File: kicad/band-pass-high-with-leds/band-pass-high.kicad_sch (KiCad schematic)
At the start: 66 parts, among them J1 Conn_01x06

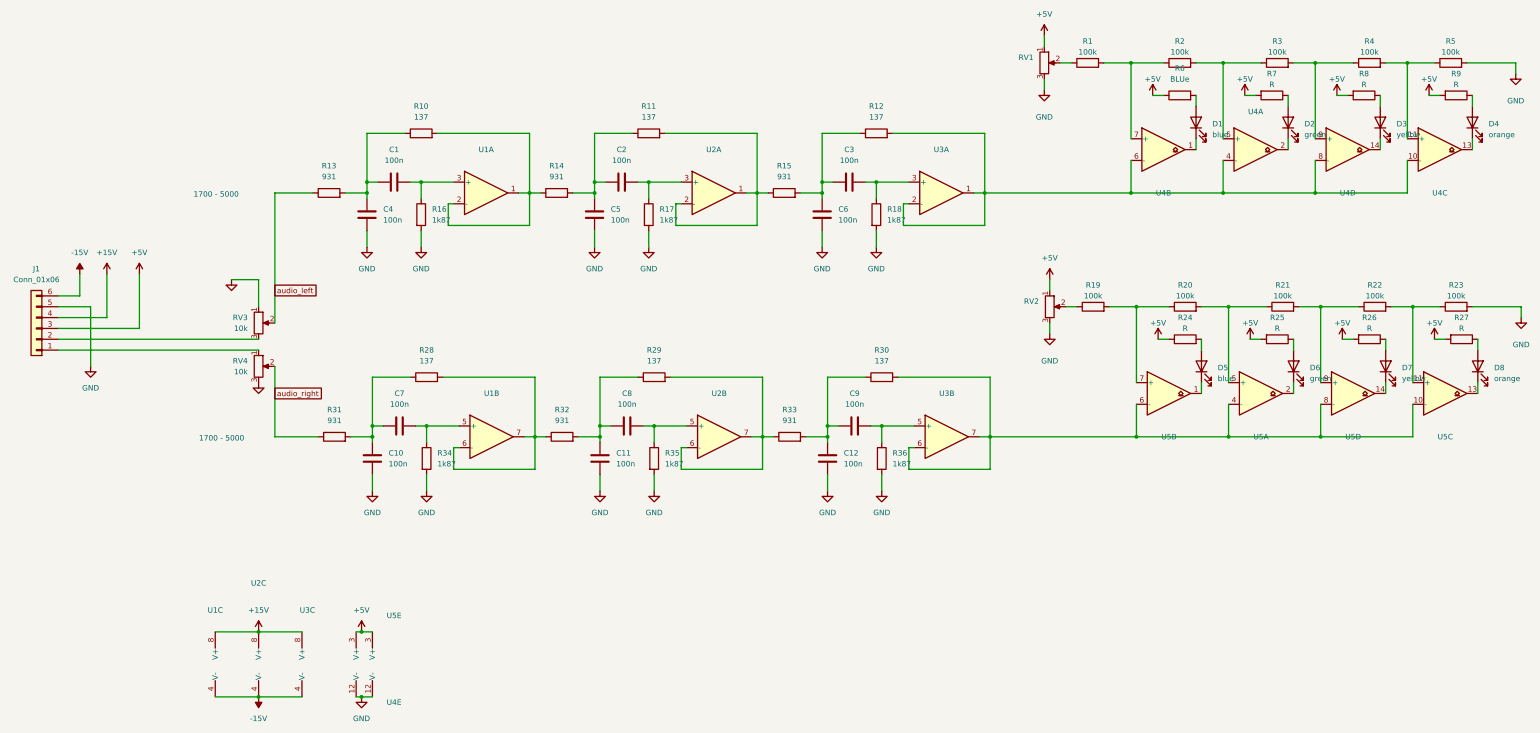
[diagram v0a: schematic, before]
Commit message: Made a filter PCB design
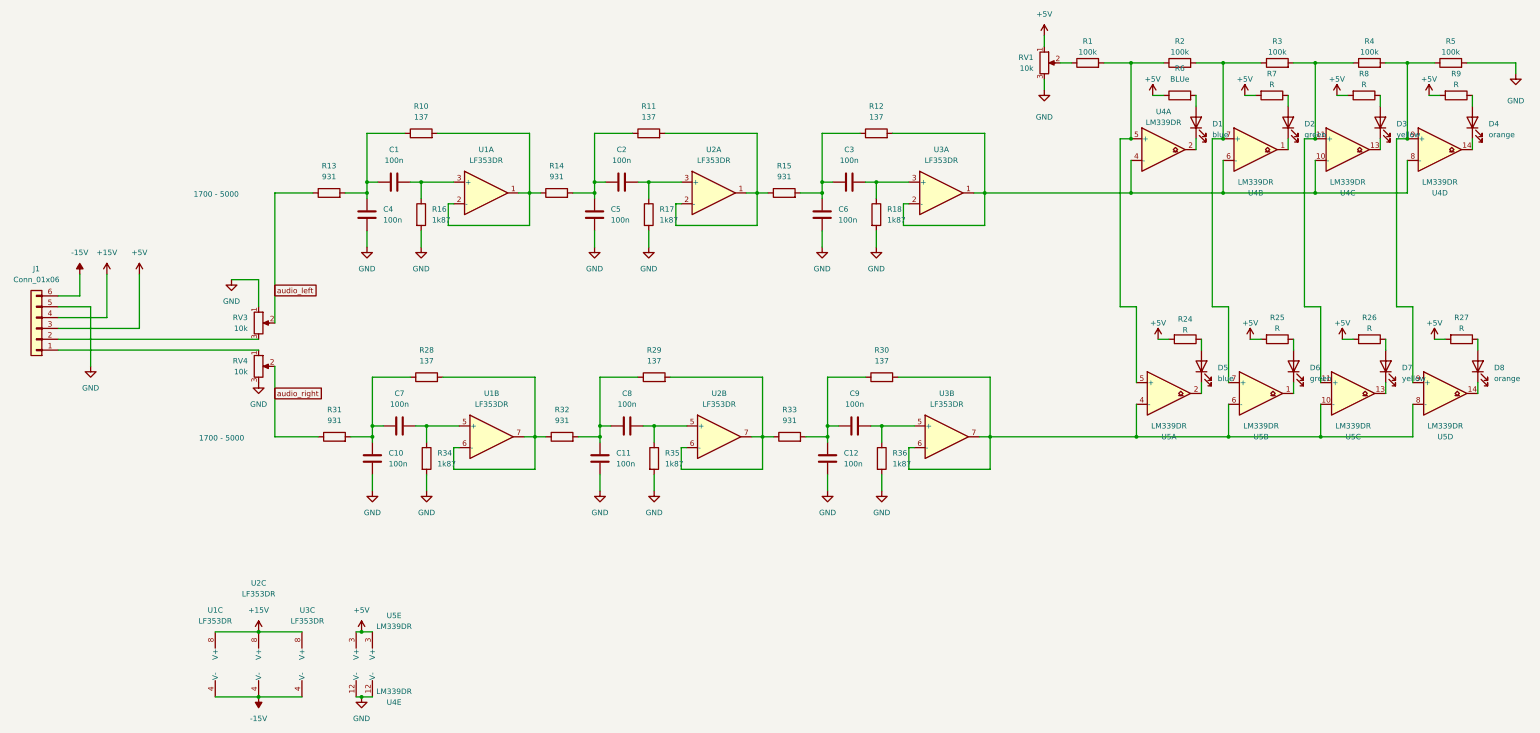
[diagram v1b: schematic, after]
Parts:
- removed R19, R20, R21, R22, R23: 100k, symbol Device:R
- removed RV2: (no value), symbol Device:R_Potentiometer
- D1, D2, D3, D4, D5, D6, D7, D8, R1, R10, R11, R12, R13, R14, R15, R16, R17, R18, R2, R24, R25, R26, R27, R28, R29, R3, R30, R31, R32, R33, R34, R35, R36, R4, R5, R6, R7, R8, R9: footprint (none) -> Resistor_SMD:R_1206_3216Metric
- J1: footprint (none) -> Connector_PinHeader_2.54mm:PinHeader_1x06_P2.54mm_Horizontal
- RV1: value (none) -> 10k; footprint (none) -> Potentiometer_THT:Potentiometer_Runtron_RM-065_Vertical
- U1, U2, U3: value (none) -> LF353DR; footprint (none) -> Package_SO:SOIC-8_3.9x4.9mm_P1.27mm
- U4, U5: value (none) -> LM339DR; footprint (none) -> Package_SO:SO-14_3.9x8.65mm_P1.27mm
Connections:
- net +5V: now also R24.2; no longer R24.1
- net at U5.5 (+): now also R1.2, R2.1, U4.5 (+)
- net at U5.9 (+): now also R4.2, R5.1, U4.9 (+)
- net at U5.7 (+): now also R2.2, R3.1, U4.7 (+)
- net at D2.1 (K): now also U4.1; no longer U4.2
- net at R3.2, R4.1: now also U4.11 (+), U5.11 (+); no longer U4.9 (+)
- net at D1.1 (K): now also U4.2; no longer U4.1
- net at D8.1 (K): now also U5.14; no longer U5.13
- net at D7.1 (K): now also U5.13; no longer U5.14
- net at U4.14: now also D4.1 (K); no longer D3.1 (K)
- net at D6.1 (K): now also U5.1; no longer U5.2
- net at D5.1 (K): now also U5.2; no longer U5.1
- net at D5.2 (A): now also R24.1; no longer R24.2
- net at U4.13: now also D3.1 (K); no longer D4.1 (K)
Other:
- moved on the sheet: R24, U4A, U4B, U4C, U4D, U5A, U5B, U5C, U5D
